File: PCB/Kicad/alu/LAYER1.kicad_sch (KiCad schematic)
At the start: 4 parts, among them U29 74LS257, U30 74LS257, U31 74LS257, U32 74LS257

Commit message: UPDATE
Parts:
- added C26, C27, C28, C29: 10n, symbol Device:C
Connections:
- net GND: now also C26.2, C27.2, C28.2, C29.2
- net VCC: now also C26.1, C27.1, C28.1, C29.1

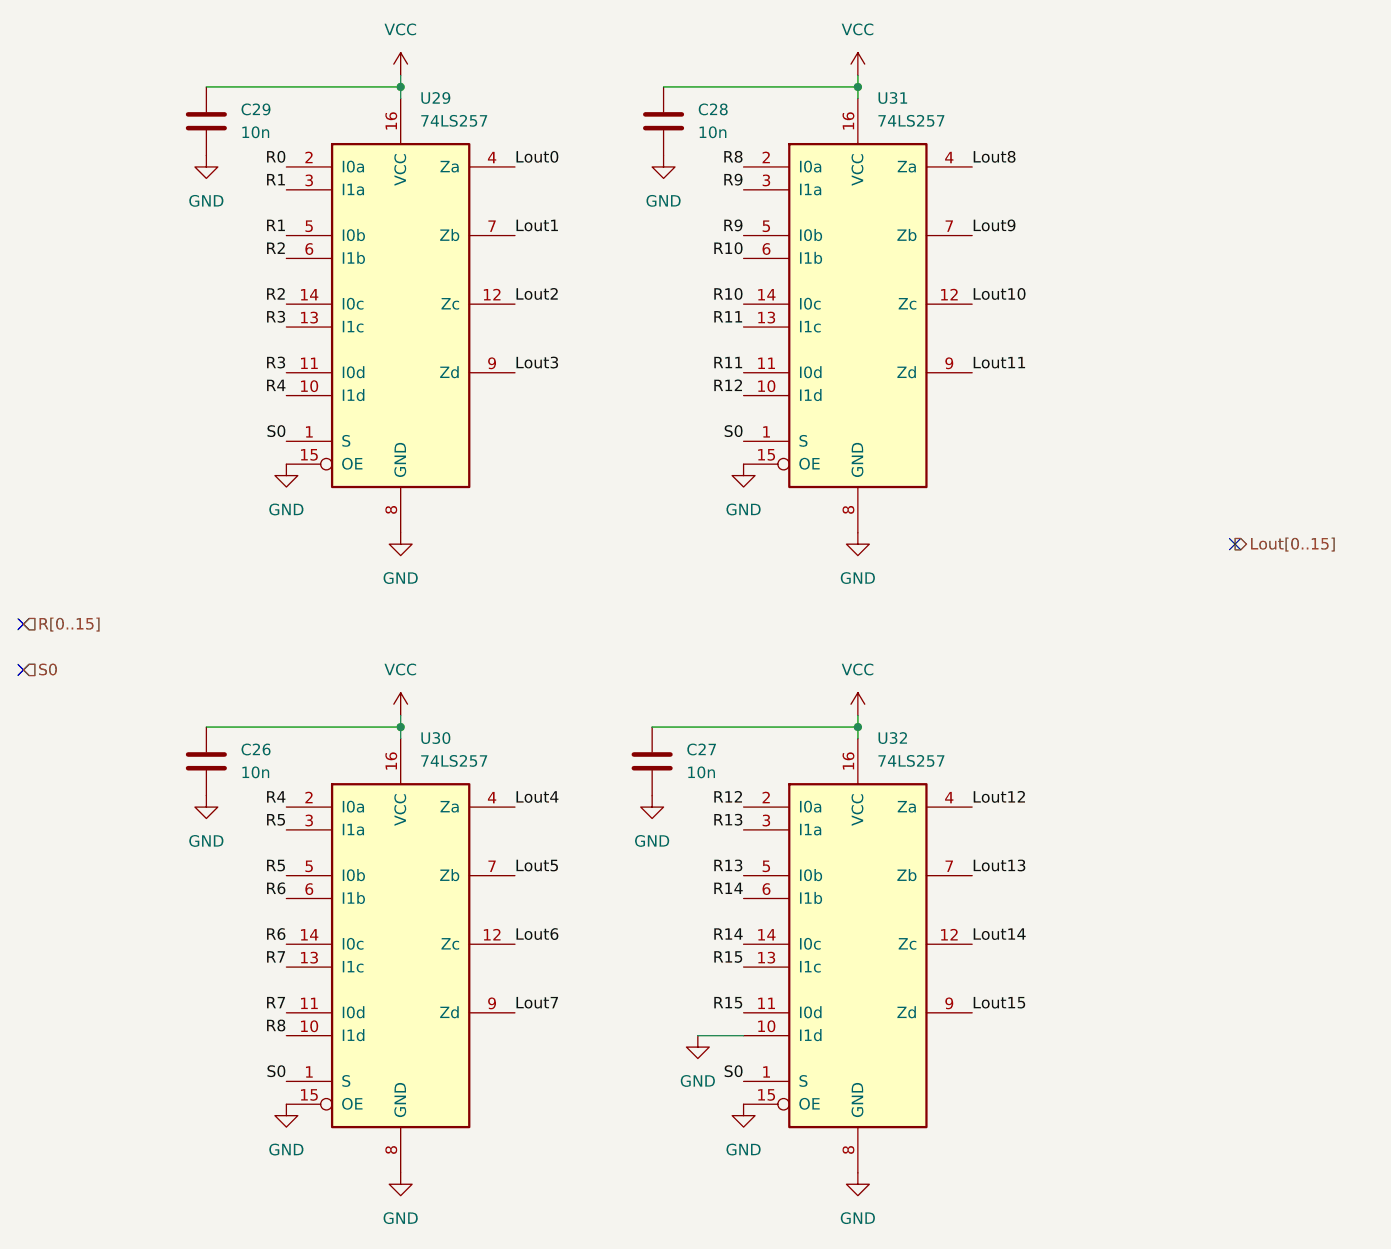
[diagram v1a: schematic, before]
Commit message: LEDs added
REGISTER.kicad_sch LEDs added to both REG_A and REG_B
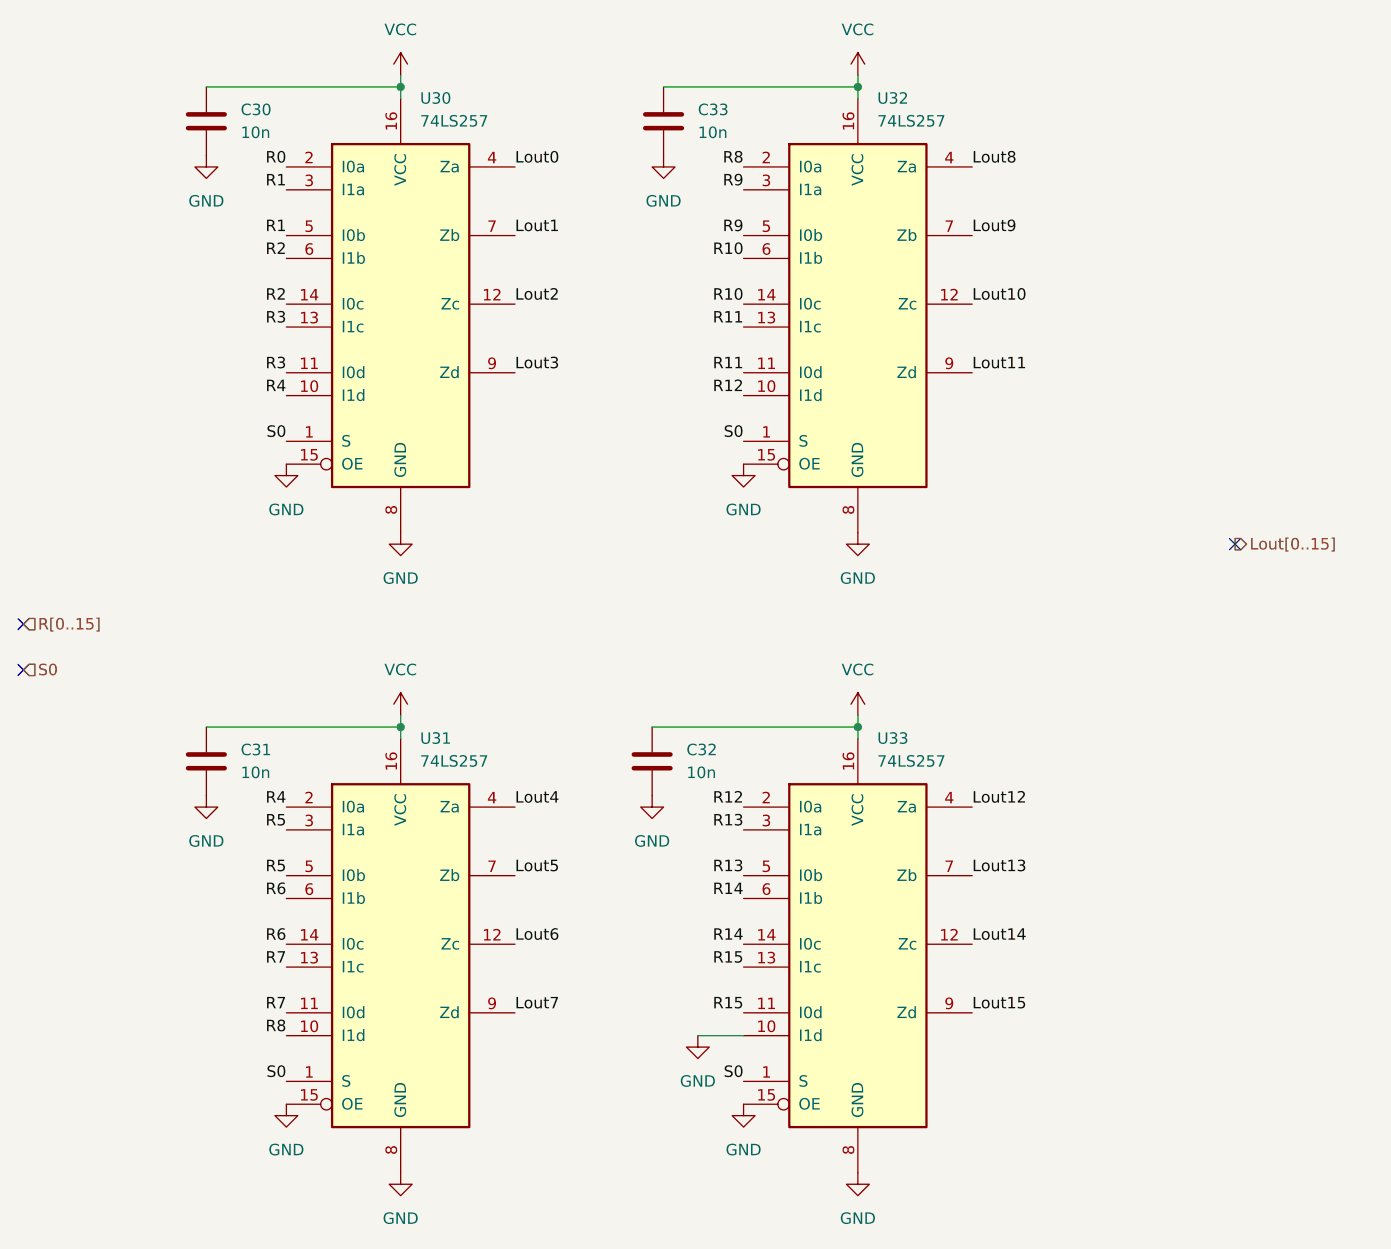
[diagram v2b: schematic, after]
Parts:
- renumbered C29 to C30, C26 to C31, C27 to C32, C28 to C33, U29 to U30, U30 to U31, U31 to U32, U32 to U33
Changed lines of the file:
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@@
 		(dnp no)
 		(fields_autoplaced yes)
-		(property "Reference" "C27"
+		(property "Reference" "C32"
 			(at 129.54 105.4099 0)
 			(effects
@@
 			(project "alu"
 				(path "/2f66781e-a1af-4159-bccc-5b52a490afb6/80a1dfcd-7697-4d3a-b862-6f8977c64ed2/dd33a53d-fe72-47cc-86dc-79380be758e3"
-					(reference "C27")
+					(reference "C32")
 					(unit 1)
 				)
@@
 		(dnp no)
 		(fields_autoplaced yes)
-		(property "Reference" "#PWR076"
+		(property "Reference" "#PWR0130"
 			(at 148.59 34.29 0)
 			(effects
@@
 			(project "alu"
 				(path "/2f66781e-a1af-4159-bccc-5b52a490afb6/80a1dfcd-7697-4d3a-b862-6f8977c64ed2/dd33a53d-fe72-47cc-86dc-79380be758e3"
-					(reference "#PWR076")
+					(reference "#PWR0130")
 					(unit 1)
 				)
@@
 		(dnp no)
 		(fields_autoplaced yes)
-		(property "Reference" "#PWR086"
+		(property "Reference" "#PWR0127"
 			(at 130.81 143.51 0)
 			(effects
@@
 			(project "alu"
 				(path "/2f66781e-a1af-4159-bccc-5b52a490afb6/80a1dfcd-7697-4d3a-b862-6f8977c64ed2/dd33a53d-fe72-47cc-86dc-79380be758e3"
-					(reference "#PWR086")
+					(reference "#PWR0127")
 					(unit 1)
 				)
@@
 		(dnp no)
 		(fields_autoplaced yes)
-		(property "Reference" "U32"
+		(property "Reference" "U33"
 			(at 150.7333 104.14 0)
 			(effects
@@
 			(project "alu"
 				(path "/2f66781e-a1af-4159-bccc-5b52a490afb6/80a1dfcd-7697-4d3a-b862-6f8977c64ed2/dd33a53d-fe72-47cc-86dc-79380be758e3"
-					(reference "U32")
+					(reference "U33")
 					(unit 1)
 				)
@@
 		(dnp no)
 		(fields_autoplaced yes)
-		(property "Reference" "U29"
+		(property "Reference" "U30"
 			(at 99.9333 33.02 0)
 			(effects
@@
 			(project ""
 				(path "/2f66781e-a1af-4159-bccc-5b52a490afb6/80a1dfcd-7697-4d3a-b862-6f8977c64ed2/dd33a53d-fe72-47cc-86dc-79380be758e3"
-					(reference "U29")
+					(reference "U30")
 					(unit 1)
 				)
@@
 		(dnp no)
 		(fields_autoplaced yes)
-		(property "Reference" "#PWR084"
+		(property "Reference" "#PWR0128"
 			(at 135.89 80.01 0)
 			(effects
@@
 			(project "alu"
 				(path "/2f66781e-a1af-4159-bccc-5b52a490afb6/80a1dfcd-7697-4d3a-b862-6f8977c64ed2/dd33a53d-fe72-47cc-86dc-79380be758e3"
-					(reference "#PWR084")
+					(reference "#PWR0128")
 					(unit 1)
 				)
@@
 		(dnp no)
 		(fields_autoplaced yes)
-		(property "Reference" "U30"
+		(property "Reference" "U31"
 			(at 99.9333 104.14 0)
 			(effects
@@
 			(project "alu"
 				(path "/2f66781e-a1af-4159-bccc-5b52a490afb6/80a1dfcd-7697-4d3a-b862-6f8977c64ed2/dd33a53d-fe72-47cc-86dc-79380be758e3"
-					(reference "U30")
+					(reference "U31")
 					(unit 1)
 				)
@@
 		(dnp no)
 		(fields_autoplaced yes)
-		(property "Reference" "#PWR0238"
+		(property "Reference" "#PWR0126"
 			(at 127 45.72 0)
 			(effects
@@
 			(project "alu"
 				(path "/2f66781e-a1af-4159-bccc-5b52a490afb6/80a1dfcd-7697-4d3a-b862-6f8977c64ed2/dd33a53d-fe72-47cc-86dc-79380be758e3"
-					(reference "#PWR0238")
+					(reference "#PWR0126")
 					(unit 1)
 				)
@@
 		(dnp no)
 		(fields_autoplaced yes)
-		(property "Reference" "C26"
+		(property "Reference" "C31"
 			(at 80.01 105.4099 0)
 			(effects
@@
 			(project "alu"
 				(path "/2f66781e-a1af-4159-bccc-5b52a490afb6/80a1dfcd-7697-4d3a-b862-6f8977c64ed2/dd33a53d-fe72-47cc-86dc-79380be758e3"
-					(reference "C26")
+					(reference "C31")
 					(unit 1)
 				)
@@
 		(dnp no)
 		(fields_autoplaced yes)
-		(property "Reference" "#PWR069"
+		(property "Reference" "#PWR0124"
 			(at 97.79 158.75 0)
 			(effects
@@
 			(project "alu"
 				(path "/2f66781e-a1af-4159-bccc-5b52a490afb6/80a1dfcd-7697-4d3a-b862-6f8977c64ed2/dd33a53d-fe72-47cc-86dc-79380be758e3"
-					(reference "#PWR069")
+					(reference "#PWR0124")
 					(unit 1)
 				)
@@
 		(dnp no)
 		(fields_autoplaced yes)
-		(property "Reference" "#PWR070"
+		(property "Reference" "#PWR0132"
 			(at 148.59 105.41 0)
 			(effects
@@
 			(project ""
 				(path "/2f66781e-a1af-4159-bccc-5b52a490afb6/80a1dfcd-7697-4d3a-b862-6f8977c64ed2/dd33a53d-fe72-47cc-86dc-79380be758e3"
-					(reference "#PWR070")
+					(reference "#PWR0132")
 					(unit 1)
 				)
@@
 		(dnp no)
 		(fields_autoplaced yes)
-		(property "Reference" "#PWR077"
+		(property "Reference" "#PWR0121"
 			(at 97.79 34.29 0)
 			(effects
@@
 			(project "alu"
 				(path "/2f66781e-a1af-4159-bccc-5b52a490afb6/80a1dfcd-7697-4d3a-b862-6f8977c64ed2/dd33a53d-fe72-47cc-86dc-79380be758e3"
-					(reference "#PWR077")
+					(reference "#PWR0121")
 					(unit 1)
 				)
@@
 		(dnp no)
 		(fields_autoplaced yes)
-		(property "Reference" "#PWR071"
+		(property "Reference" "#PWR0123"
 			(at 97.79 105.41 0)
 			(effects
@@
 			(project "alu"
 				(path "/2f66781e-a1af-4159-bccc-5b52a490afb6/80a1dfcd-7697-4d3a-b862-6f8977c64ed2/dd33a53d-fe72-47cc-86dc-79380be758e3"
-					(reference "#PWR071")
+					(reference "#PWR0123")
 					(unit 1)
 				)
@@
 		(dnp no)
 		(fields_autoplaced yes)
-		(property "Reference" "#PWR0237"
+		(property "Reference" "#PWR0125"
 			(at 125.73 116.84 0)
 			(effects
@@
 			(project "alu"
 				(path "/2f66781e-a1af-4159-bccc-5b52a490afb6/80a1dfcd-7697-4d3a-b862-6f8977c64ed2/dd33a53d-fe72-47cc-86dc-79380be758e3"
-					(reference "#PWR0237")
+					(reference "#PWR0125")
 					(unit 1)
 				)
@@
 		(dnp no)
 		(fields_autoplaced yes)
-		(property "Reference" "#PWR063"
+		(property "Reference" "#PWR0131"
 			(at 148.59 87.63 0)
 			(effects
@@
 			(project "alu"
 				(path "/2f66781e-a1af-4159-bccc-5b52a490afb6/80a1dfcd-7697-4d3a-b862-6f8977c64ed2/dd33a53d-fe72-47cc-86dc-79380be758e3"
-					(reference "#PWR063")
+					(reference "#PWR0131")
 					(unit 1)
 				)
@@
 		(dnp no)
 		(fields_autoplaced yes)
-		(property "Reference" "#PWR0236"
+		(property "Reference" "#PWR0118"
 			(at 76.2 116.84 0)
 			(effects
@@
 			(project "alu"
 				(path "/2f66781e-a1af-4159-bccc-5b52a490afb6/80a1dfcd-7697-4d3a-b862-6f8977c64ed2/dd33a53d-fe72-47cc-86dc-79380be758e3"
-					(reference "#PWR0236")
+					(reference "#PWR0118")
 					(unit 1)
 				)
@@
 		(dnp no)
 		(fields_autoplaced yes)
-		(property "Reference" "#PWR062"
+		(property "Reference" "#PWR0122"
 			(at 97.79 87.63 0)
 			(effects
@@
 			(project ""
 				(path "/2f66781e-a1af-4159-bccc-5b52a490afb6/80a1dfcd-7697-4d3a-b862-6f8977c64ed2/dd33a53d-fe72-47cc-86dc-79380be758e3"
-					(reference "#PWR062")
+					(reference "#PWR0122")
 					(unit 1)
 				)
@@
 		(dnp no)
 		(fields_autoplaced yes)
-		(property "Reference" "#PWR085"
+		(property "Reference" "#PWR0119"
 			(at 85.09 80.01 0)
 			(effects
@@
 			(project "alu"
 				(path "/2f66781e-a1af-4159-bccc-5b52a490afb6/80a1dfcd-7697-4d3a-b862-6f8977c64ed2/dd33a53d-fe72-47cc-86dc-79380be758e3"
-					(reference "#PWR085")
+					(reference "#PWR0119")
 					(unit 1)
 				)
@@
 		(dnp no)
 		(fields_autoplaced yes)
-		(property "Reference" "#PWR068"
+		(property "Reference" "#PWR0133"
 			(at 148.59 158.75 0)
 			(effects
@@
 			(project "alu"
 				(path "/2f66781e-a1af-4159-bccc-5b52a490afb6/80a1dfcd-7697-4d3a-b862-6f8977c64ed2/dd33a53d-fe72-47cc-86dc-79380be758e3"
-					(reference "#PWR068")
+					(reference "#PWR0133")
 					(unit 1)
 				)
@@
 		(dnp no)
 		(fields_autoplaced yes)
-		(property "Reference" "#PWR079"
+		(property "Reference" "#PWR0129"
 			(at 135.89 151.13 0)
 			(effects
@@
 			(project "alu"
 				(path "/2f66781e-a1af-4159-bccc-5b52a490afb6/80a1dfcd-7697-4d3a-b862-6f8977c64ed2/dd33a53d-fe72-47cc-86dc-79380be758e3"
-					(reference "#PWR079")
+					(reference "#PWR0129")
 					(unit 1)
 				)
@@
 		(dnp no)
 		(fields_autoplaced yes)
-		(property "Reference" "U31"
+		(property "Reference" "U32"
 			(at 150.7333 33.02 0)
 			(effects
@@
 			(project "alu"
 				(path "/2f66781e-a1af-4159-bccc-5b52a490afb6/80a1dfcd-7697-4d3a-b862-6f8977c64ed2/dd33a53d-fe72-47cc-86dc-79380be758e3"
-					(reference "U31")
+					(reference "U32")
 					(unit 1)
 				)
@@
 		(dnp no)
 		(fields_autoplaced yes)
-		(property "Reference" "C29"
+		(property "Reference" "C30"
 			(at 80.01 34.2899 0)
 			(effects
@@
 			(project "alu"
 				(path "/2f66781e-a1af-4159-bccc-5b52a490afb6/80a1dfcd-7697-4d3a-b862-6f8977c64ed2/dd33a53d-fe72-47cc-86dc-79380be758e3"
-					(reference "C29")
+					(reference "C30")
 					(unit 1)
 				)
@@
 		(dnp no)
 		(fields_autoplaced yes)
-		(property "Reference" "#PWR078"
+		(property "Reference" "#PWR0120"
 			(at 85.09 151.13 0)
 			(effects
@@
 			(project "alu"
 				(path "/2f66781e-a1af-4159-bccc-5b52a490afb6/80a1dfcd-7697-4d3a-b862-6f8977c64ed2/dd33a53d-fe72-47cc-86dc-79380be758e3"
-					(reference "#PWR078")
+					(reference "#PWR0120")
 					(unit 1)
 				)
@@
 		(dnp no)
 		(fields_autoplaced yes)
-		(property "Reference" "#PWR0239"
+		(property "Reference" "#PWR0117"
 			(at 76.2 45.72 0)
 			(effects
@@
 			(project "alu"
 				(path "/2f66781e-a1af-4159-bccc-5b52a490afb6/80a1dfcd-7697-4d3a-b862-6f8977c64ed2/dd33a53d-fe72-47cc-86dc-79380be758e3"
-					(reference "#PWR0239")
+					(reference "#PWR0117")
 					(unit 1)
 				)
@@
 		(dnp no)
 		(fields_autoplaced yes)
-		(property "Reference" "C28"
+		(property "Reference" "C33"
 			(at 130.81 34.2899 0)
 			(effects
@@
 			(project "alu"
 				(path "/2f66781e-a1af-4159-bccc-5b52a490afb6/80a1dfcd-7697-4d3a-b862-6f8977c64ed2/dd33a53d-fe72-47cc-86dc-79380be758e3"
-					(reference "C28")
-					(unit 1)
-				)
+					(reference "C33")
+					(unit 1)
+				)

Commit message: Footprints, PCB update
Added footprints to all components, updated the PCB with the schematic
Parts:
- C30, C31, C32, C33: footprint (none) -> Capacitor_SMD:C_0603_1608Metric
- U30, U31, U32, U33: footprint (none) -> Package_SO:SOIC-16_3.9x9.9mm_P1.27mm
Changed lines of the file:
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@@
 			)
 		)
-		(property "Footprint" ""
+		(property "Footprint" "Capacitor_SMD:C_0603_1608Metric"
 			(at 126.6952 110.49 0)
 			(effects
@@
 			)
 		)
-		(property "Footprint" ""
+		(property "Footprint" "Package_SO:SOIC-16_3.9x9.9mm_P1.27mm"
 			(at 148.59 127 0)
 			(effects
@@
 			)
 		)
-		(property "Footprint" ""
+		(property "Footprint" "Package_SO:SOIC-16_3.9x9.9mm_P1.27mm"
 			(at 97.79 55.88 0)
 			(effects
@@
 			)
 		)
-		(property "Footprint" ""
+		(property "Footprint" "Package_SO:SOIC-16_3.9x9.9mm_P1.27mm"
 			(at 97.79 127 0)
 			(effects
@@
 			)
 		)
-		(property "Footprint" ""
+		(property "Footprint" "Capacitor_SMD:C_0603_1608Metric"
 			(at 77.1652 110.49 0)
 			(effects
@@
 			)
 		)
-		(property "Footprint" ""
+		(property "Footprint" "Package_SO:SOIC-16_3.9x9.9mm_P1.27mm"
 			(at 148.59 55.88 0)
 			(effects
@@
 			)
 		)
-		(property "Footprint" ""
+		(property "Footprint" "Capacitor_SMD:C_0603_1608Metric"
 			(at 77.1652 39.37 0)
 			(effects
@@
 			)
 		)
-		(property "Footprint" ""
+		(property "Footprint" "Capacitor_SMD:C_0603_1608Metric"
 			(at 127.9652 39.37 0)
 			(effects

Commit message: ALU Pcb update
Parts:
- C30, C31, C32, C33: value 10n -> 100nF; footprint Capacitor_SMD:C_0603_1608Metric -> Capacitor_SMD:C_0402_1005Metric
- U30, U31, U32, U33: value 74LS257 -> 74257
